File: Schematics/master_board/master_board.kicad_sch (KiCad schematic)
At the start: 44 parts, among them J1 2x5x1.27mm, J2 USB_C_Receptacle_USB2.0, SW1 SW_Push, SW2 SW_Push, U1 NCP1117-3.3_SOT223, U2 RP2040, U3 W25Q16JVSSIQ, Y1 ABLS-12.000MHZ-B4-T

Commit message: Footprint integration
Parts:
- added U4, U5: 316040001, symbol merricks_lib:316040001
- gave numbers to parts that had none: 3
- renumbered C11 to C10, C12 to C11, C5 to C4, C6 to C5, C7 to C6, C8 to C7, C9 to C8, C10 to C9, R5 to R12, R1 to R7, R2 to R8, R4 to R9
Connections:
- net GND: now also U4.2 (GND), U5.2 (GND)
- net GPIO5: now also R16.1
- net GPIO6: now also R17.1
- net at R16.2: now also U4.1 (VCC)
- net at R17.2: now also U5.1 (VCC)
- net GPIO10 renamed A2
- net GPIO11 renamed A1
- net GPIO12 renamed A0
- net GPIO16 renamed SPI0_RX
- net GPIO18 renamed SPI0_SCLK
- net GPIO19 renamed SPI0_TX
- net GPIO7 renamed E0N_B
- net GPIO8 renamed E0N_A
- net GPIO9 renamed A3
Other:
- note added: "HAPTIC FEEDBACK"
- note added: "MODULE DECODER"
- moved on the sheet: C12, C13, R14, Y1

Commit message: Added footprints to resistors, capcacitors, potentiometers, etc.
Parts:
- SW1, SW2, SW3: footprint (none) -> Button_Switch_THT:Push_E-Switch_KS01Q01
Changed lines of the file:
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@@
     (property "Reference" "SW2" (id 0) (at 127 175.26 0))
     (property "Value" "SW_Push" (id 1) (at 127 182.88 0))
-    (property "Footprint" "" (id 2) (at 127 175.26 0)
+    (property "Footprint" "Button_Switch_THT:Push_E-Switch_KS01Q01" (id 2) (at 127 175.26 0)
       (effects (font (size 1.27 1.27)) hide)
     )
@@
     (property "Reference" "SW1" (id 0) (at 91.44 175.26 0))
     (property "Value" "SW_Push" (id 1) (at 91.44 182.88 0))
-    (property "Footprint" "" (id 2) (at 91.44 175.26 0)
+    (property "Footprint" "Button_Switch_THT:Push_E-Switch_KS01Q01" (id 2) (at 91.44 175.26 0)
       (effects (font (size 1.27 1.27)) hide)
     )
@@
     (property "Reference" "SW3" (id 0) (at 162.56 175.26 0))
     (property "Value" "SW_Push" (id 1) (at 162.56 182.88 0))
-    (property "Footprint" "" (id 2) (at 162.56 175.26 0)
+    (property "Footprint" "Button_Switch_THT:Push_E-Switch_KS01Q01" (id 2) (at 162.56 175.26 0)
       (effects (font (size 1.27 1.27)) hide)
     )
@@
     )
     (path "/a524c91f-ff5d-4073-ae0f-6cfe00c0490f"
-      (reference "SW1") (unit 1) (value "SW_Push") (footprint "")
+      (reference "SW1") (unit 1) (value "SW_Push") (footprint "Button_Switch_THT:Push_E-Switch_KS01Q01")
     )
     (path "/85907b86-3c20-4a7d-b80b-57a92e4b78e0"
-      (reference "SW2") (unit 1) (value "SW_Push") (footprint "")
+      (reference "SW2") (unit 1) (value "SW_Push") (footprint "Button_Switch_THT:Push_E-Switch_KS01Q01")
     )
     (path "/e0b93d9d-7fc1-466a-81e7-491989a0b279"
-      (reference "SW3") (unit 1) (value "SW_Push") (footprint "")
+      (reference "SW3") (unit 1) (value "SW_Push") (footprint "Button_Switch_THT:Push_E-Switch_KS01Q01")
     )
     (path "/f0ce6264-04dc-4a7e-a059-fc852e5bd7d4"

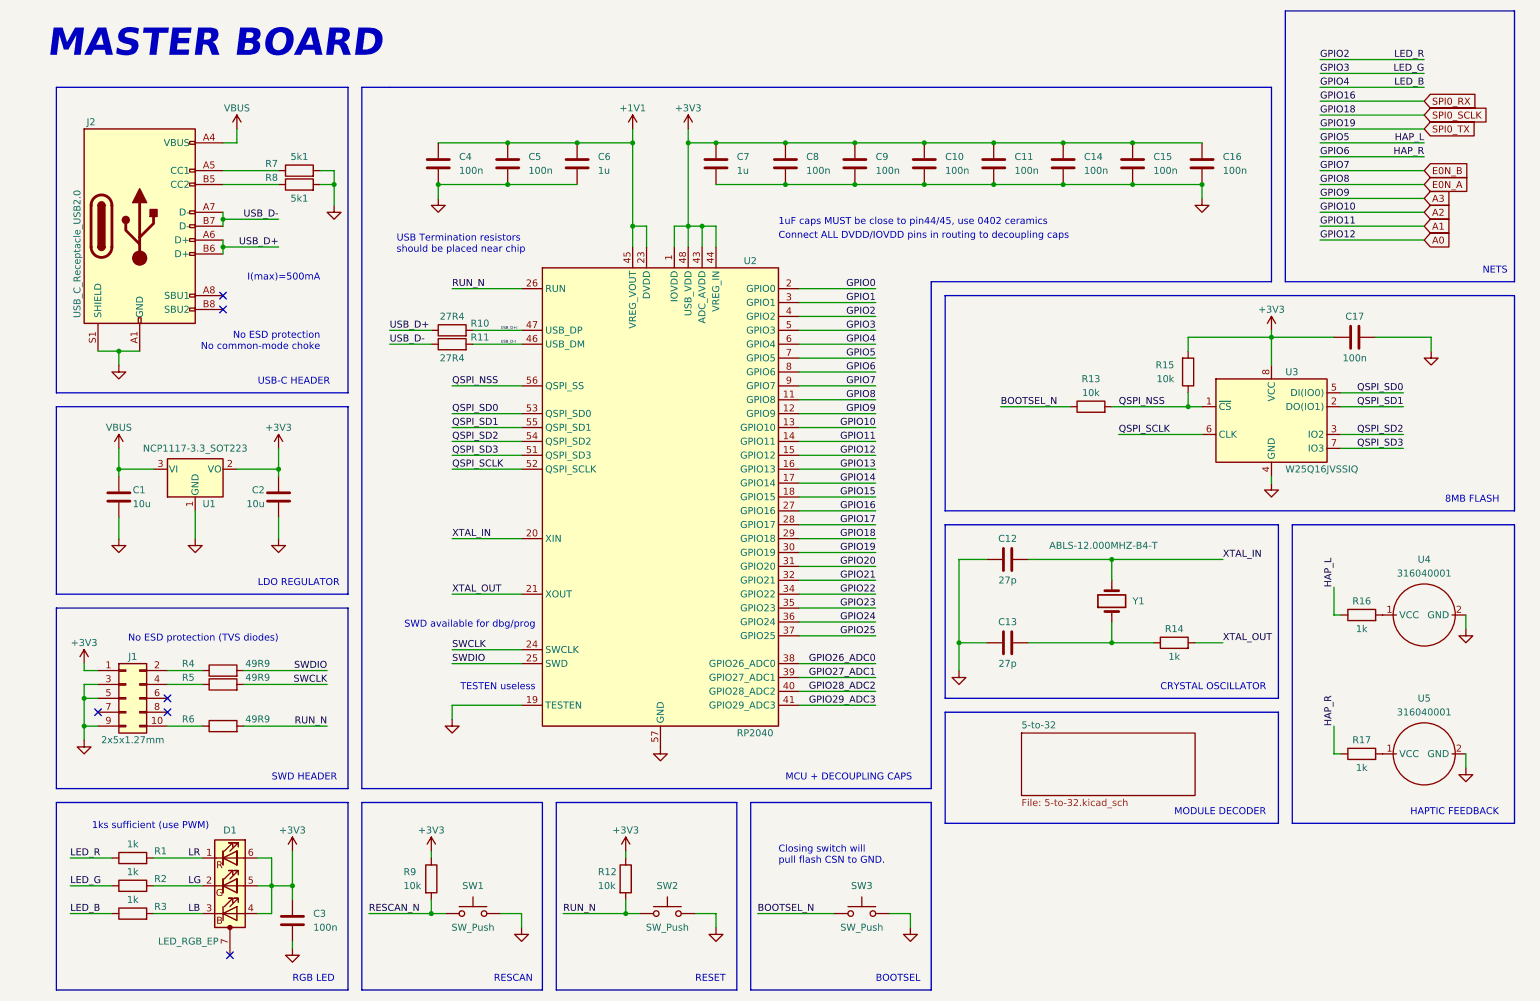
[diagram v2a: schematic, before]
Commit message: Master board connectors and ERC
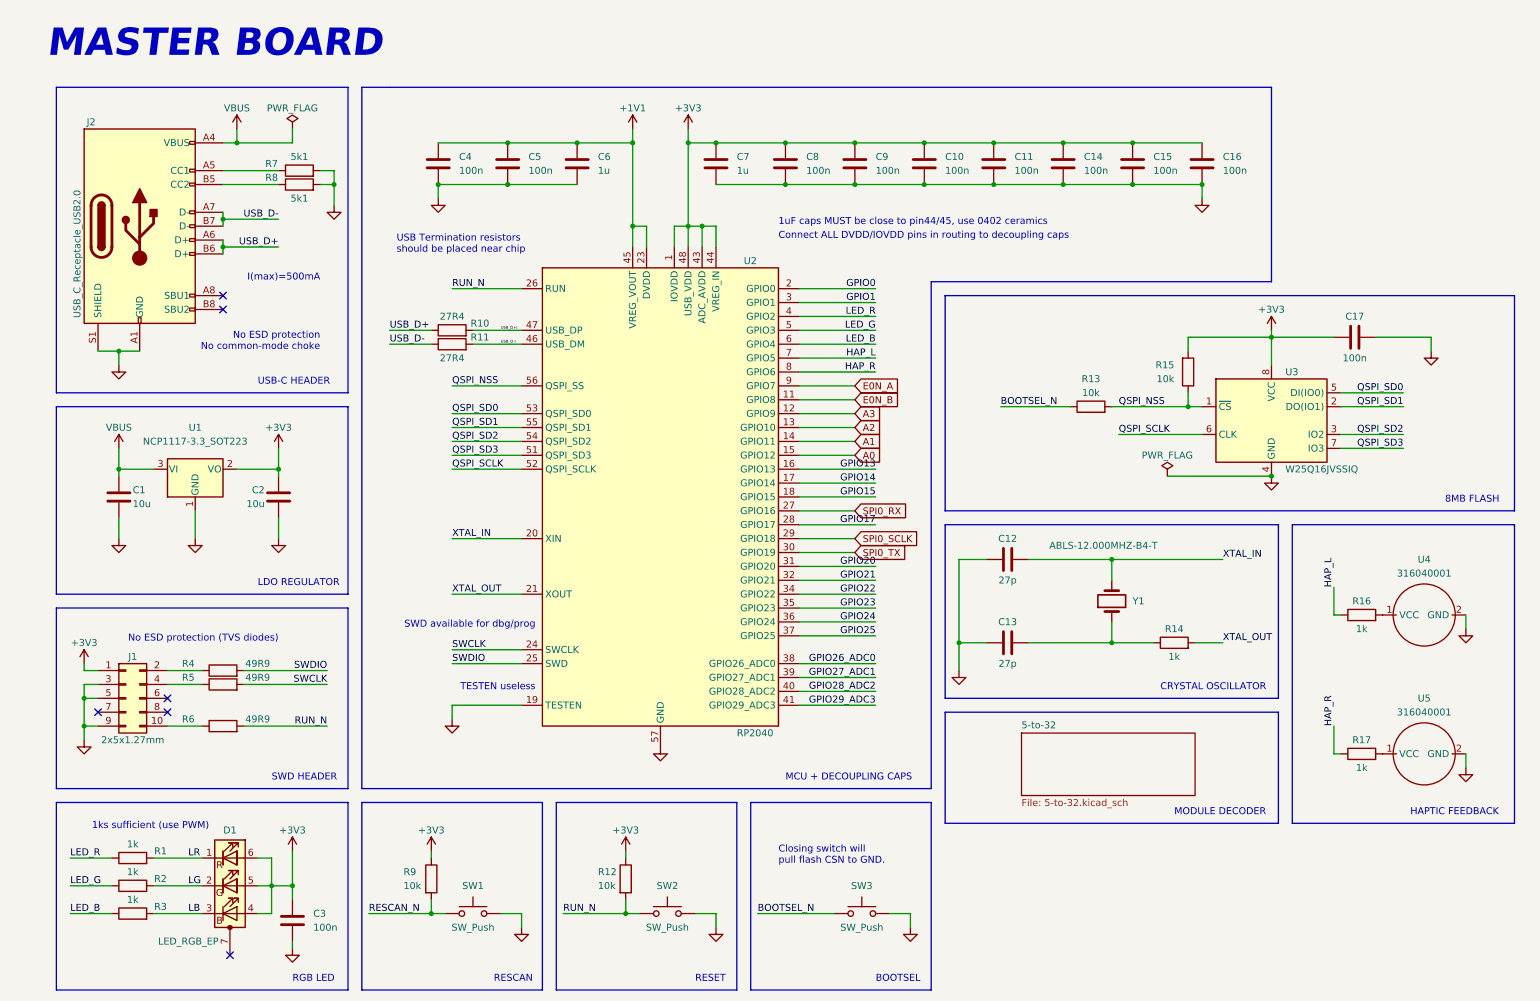
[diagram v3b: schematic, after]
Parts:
- removed U3: W25Q16JVSSIQ, W25Q16JVSSIQ:SOIC127P790X216-8N, symbol Merrick_Symbols_KiCad6:W25Q16JVSSIQ
- added U3: W25Q16JVSSIQ, Package_SO:SOIC-8_5.23x5.23mm_P1.27mm, symbol prototroller_symbols:W25Q16JVSSIQ
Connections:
- net +3V3: now also U3.8 (VCC)
- net E0N_A: now also U2.9 (GPIO7); no longer U2.11 (GPIO8)
- net E0N_B: now also U2.11 (GPIO8); no longer U2.9 (GPIO7)
- net GND: now also U3.4 (GND)
- net QSPI_NSS: now also U3.1 (~{CS})
- net QSPI_SCLK: now also U3.6 (CLK)
- net QSPI_SD0: now also U3.5 (DI(IO0))
- net QSPI_SD1: now also U3.2 (DO(IO1))
- net QSPI_SD2: now also U3.3 (IO2)
- net QSPI_SD3: now also U3.7 (IO3)
- net GPIO2 renamed LED_R
- net GPIO3 renamed LED_G
- net GPIO4 renamed LED_B
- net GPIO5 renamed HAP_L
- net GPIO6 renamed HAP_R
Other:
- note removed: "NETS"

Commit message: Update footprints
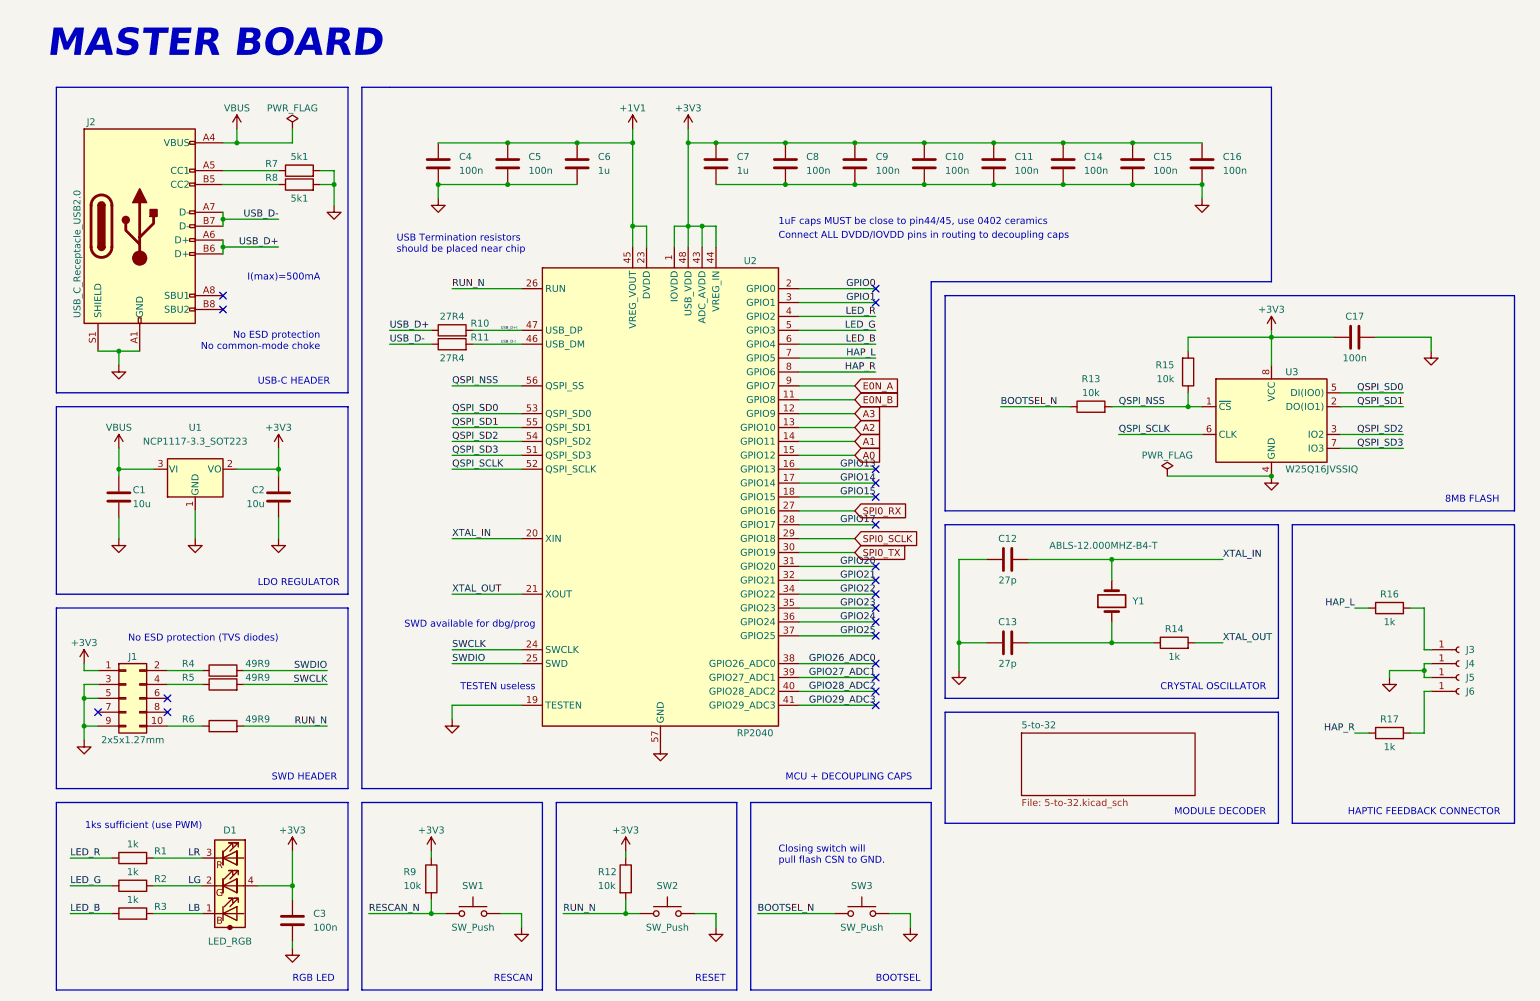
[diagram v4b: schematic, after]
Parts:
- removed D1: LED_RGB_EP, symbol Device:LED_RGB_EP
- removed U4, U5: 316040001, symbol merricks_lib:316040001
- added D1: LED_RGB, prototroller_footprints:LED_Cree-UHD111A, symbol prototroller_symbols:LED_RGB
- added J3, J4, J5, J6: Conn_01x01_Female, Connector_PinHeader_2.54mm:PinHeader_1x01_P2.54mm_Vertical, symbol Connector:Conn_01x01_Female
- J1: footprint Connector_PinHeader_1.27mm:PinHeader_2x05_P1.27mm_Vertical -> Connector_PinHeader_1.27mm:PinHeader_2x05_P1.27mm_Vertical_SMD
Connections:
- net +3V3: now also D1.4 (A)
- net GND: now also J4.1 (Pin_1), J5.1 (Pin_1)
- net LB: now also D1.1 (B)
- net LG: now also D1.2 (G)
- net LR: now also D1.3 (R)
- net at R17.2: now also J6.1 (Pin_1)
- net at R16.2: now also J3.1 (Pin_1)
- no-connect marks 6 -> 21
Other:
- note added: "HAPTIC FEEDBACK CONNECTOR"
- note removed: "HAPTIC FEEDBACK"
- moved on the sheet: R16, R17

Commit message: Initial master board placement
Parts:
- J2: footprint Connector_USB:USB_C_Plug_Molex_105444 -> Connector_USB:USB_C_Receptacle_GCT_USB4105-xx-A_16P_TopMnt_Horizontal
- SW1, SW2, SW3: footprint Button_Switch_THT:Push_E-Switch_KS01Q01 -> prototroller_footprints:Switch_D6C40F1LFS
- Y1: footprint ABLS-12:XTAL_ABLS-12.000MHZ-B4-T -> prototroller_footprints:XTAL_ABLS-12.000MHZ-B4-T
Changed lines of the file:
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@@
     (property "Reference" "SW2" (id 0) (at 127 175.26 0))
     (property "Value" "SW_Push" (id 1) (at 127 182.88 0))
-    (property "Footprint" "Button_Switch_THT:Push_E-Switch_KS01Q01" (id 2) (at 127 175.26 0)
+    (property "Footprint" "prototroller_footprints:Switch_D6C40F1LFS" (id 2) (at 127 175.26 0)
       (effects (font (size 1.27 1.27)) hide)
     )
@@
     (property "Reference" "SW1" (id 0) (at 91.44 175.26 0))
     (property "Value" "SW_Push" (id 1) (at 91.44 182.88 0))
-    (property "Footprint" "Button_Switch_THT:Push_E-Switch_KS01Q01" (id 2) (at 91.44 175.26 0)
+    (property "Footprint" "prototroller_footprints:Switch_D6C40F1LFS" (id 2) (at 91.44 175.26 0)
       (effects (font (size 1.27 1.27)) hide)
     )
@@
     (property "Reference" "J2" (id 0) (at 21.59 35.56 0))
     (property "Value" "USB_C_Receptacle_USB2.0" (id 1) (at 19.05 59.69 90))
-    (property "Footprint" "Connector_USB:USB_C_Plug_Molex_105444" (id 2) (at 34.29 54.61 0)
+    (property "Footprint" "Connector_USB:USB_C_Receptacle_GCT_USB4105-xx-A_16P_TopMnt_Horizontal" (id 2) (at 34.29 54.61 0)
       (effects (font (size 1.27 1.27)) hide)
     )
@@
       (effects (font (size 1.27 1.27)) (justify right))
     )
-    (property "Footprint" "ABLS-12:XTAL_ABLS-12.000MHZ-B4-T" (id 2) (at 208.28 123.19 0)
+    (property "Footprint" "prototroller_footprints:XTAL_ABLS-12.000MHZ-B4-T" (id 2) (at 208.28 123.19 0)
       (effects (font (size 1.27 1.27)) hide)
     )
@@
     (property "Reference" "SW3" (id 0) (at 162.56 175.26 0))
     (property "Value" "SW_Push" (id 1) (at 162.56 182.88 0))
-    (property "Footprint" "Button_Switch_THT:Push_E-Switch_KS01Q01" (id 2) (at 162.56 175.26 0)
+    (property "Footprint" "prototroller_footprints:Switch_D6C40F1LFS" (id 2) (at 162.56 175.26 0)
       (effects (font (size 1.27 1.27)) hide)
     )
@@
     )
     (path "/bdd9c7c5-b808-45c5-9ad6-ccf43a7c3701"
-      (reference "J2") (unit 1) (value "USB_C_Receptacle_USB2.0") (footprint "Connector_USB:USB_C_Plug_Molex_105444")
+      (reference "J2") (unit 1) (value "USB_C_Receptacle_USB2.0") (footprint "Connector_USB:USB_C_Receptacle_GCT_USB4105-xx-A_16P_TopMnt_Horizontal")
     )
     (path "/4a164639-d4bc-427a-8148-49e5a139a926"
@@
     )
     (path "/a524c91f-ff5d-4073-ae0f-6cfe00c0490f"
-      (reference "SW1") (unit 1) (value "SW_Push") (footprint "Button_Switch_THT:Push_E-Switch_KS01Q01")
+      (reference "SW1") (unit 1) (value "SW_Push") (footprint "prototroller_footprints:Switch_D6C40F1LFS")
     )
     (path "/85907b86-3c20-4a7d-b80b-57a92e4b78e0"
-      (reference "SW2") (unit 1) (value "SW_Push") (footprint "Button_Switch_THT:Push_E-Switch_KS01Q01")
+      (reference "SW2") (unit 1) (value "SW_Push") (footprint "prototroller_footprints:Switch_D6C40F1LFS")
     )
     (path "/e0b93d9d-7fc1-466a-81e7-491989a0b279"
-      (reference "SW3") (unit 1) (value "SW_Push") (footprint "Button_Switch_THT:Push_E-Switch_KS01Q01")
+      (reference "SW3") (unit 1) (value "SW_Push") (footprint "prototroller_footprints:Switch_D6C40F1LFS")
     )
     (path "/4c1ec3c1-967c-4372-8481-0e54250ca3a6"
@@
     )
     (path "/c4092f23-0ff3-4aa8-b78a-c70b581328f4"
-      (reference "Y1") (unit 1) (value "ABLS-12.000MHZ-B4-T") (footprint "ABLS-12:XTAL_ABLS-12.000MHZ-B4-T")
-    )
-  )
+      (reference "Y1") (unit 1) (value "ABLS-12.000MHZ-B4-T") (footprint "prototroller_footprints:XTAL_ABLS-12.000MHZ-B4-T")
+    )
+  )
